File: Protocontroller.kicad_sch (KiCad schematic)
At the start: 37 parts, among them U1 AP2112K-3.3TRG1, U2 PM254-1-14-Z-8.5, U3 PM254-1-14-Z-8.5, U4 SN74AHCT245PWR, U5 SN74AHCT245PWR, U6 SN74AHCT374PWR, U8 2541WR-2X08P, U9 2541WR-2X05P

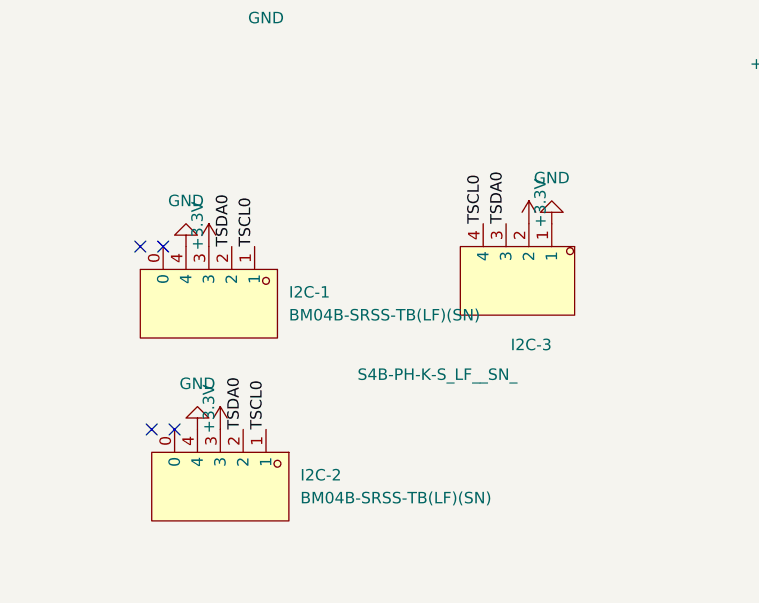
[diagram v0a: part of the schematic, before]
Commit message: Fix I2C, Pathing, and improve Silkscreen
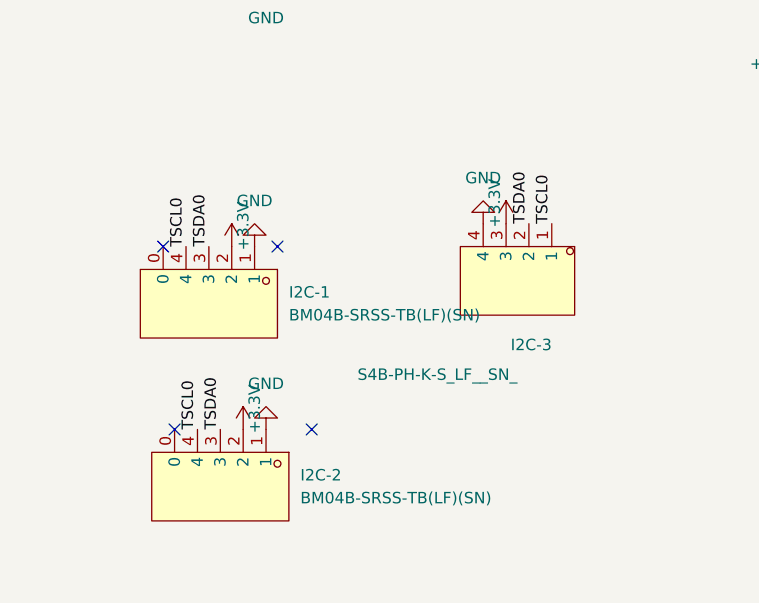
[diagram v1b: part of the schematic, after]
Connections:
- net +3.3V: now also I2C-1.2, I2C-2.2, I2C-3.3; no longer I2C-1.3, I2C-2.3, I2C-3.2
- net GND: now also I2C-1.1, I2C-2.1, I2C-3.4; no longer I2C-1.4, I2C-2.4, I2C-3.1
- net TSCL0: now also I2C-1.4, I2C-2.4, I2C-3.1; no longer I2C-1.1, I2C-2.1, I2C-3.4
- net TSDA0: now also I2C-1.3, I2C-2.3, I2C-3.2; no longer I2C-1.2, I2C-2.2, I2C-3.3
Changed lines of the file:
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@@
 	)
 	(no_connect
-		(at 43.18 135.89)
+		(at 60.96 135.89)
 	)
 	(no_connect
@@
 	)
 	(no_connect
-		(at 44.45 115.57)
+		(at 57.15 115.57)
 	)
 	(no_connect
@@
 	)
 	(no_connect
-		(at 41.91 115.57)
+		(at 44.45 115.57)
 	)
 	(no_connect
@@
 	)
 	(label "TSCL0"
-		(at 54.61 115.57 90)
+		(at 46.99 115.57 90)
 		(effects
 			(font
@@
 	)
 	(label "TSDA0"
-		(at 53.34 135.89 90)
+		(at 50.8 135.89 90)
 		(effects
 			(font
@@
 	)
 	(label "TSCL0"
-		(at 55.88 135.89 90)
+		(at 48.26 135.89 90)
 		(effects
 			(font
@@
 	)
 	(label "TSCL0"
-		(at 80.01 113.03 90)
+		(at 87.63 113.03 90)
 		(effects
 			(font
@@
 	)
 	(label "TSDA0"
-		(at 82.55 113.03 90)
+		(at 85.09 113.03 90)
 		(effects
 			(font
@@
 	)
 	(label "TSDA0"
-		(at 52.07 115.57 90)
+		(at 49.53 115.57 90)
 		(effects
 			(font
@@
 	(symbol
 		(lib_id "power:GND")
-		(at 48.26 135.89 180)
+		(at 55.88 135.89 0)
+		(mirror x)
 		(unit 1)
 		(exclude_from_sim no)
@@
 		(fields_autoplaced yes)
 		(property "Reference" "#PWR020"
-			(at 48.26 129.54 0)
+			(at 55.88 129.54 0)
 			(effects
 				(font
@@
 		)
 		(property "Value" "GND"
-			(at 48.26 130.81 0)
+			(at 55.88 130.81 0)
 			(effects
 				(font
@@
 		)
 		(property "Footprint" ""
-			(at 48.26 135.89 0)
+			(at 55.88 135.89 0)
 			(effects
 				(font
@@
 		)
 		(property "Datasheet" ""
-			(at 48.26 135.89 0)
+			(at 55.88 135.89 0)
 			(effects
 				(font
@@
 		)
 		(property "Description" "Power symbol creates a global label with name \"GND\" , ground"
-			(at 48.26 135.89 0)
+			(at 55.88 135.89 0)
 			(effects
 				(font
@@
 	(symbol
 		(lib_id "power:+3.3V")
-		(at 85.09 113.03 0)
-		(mirror y)
+		(at 82.55 113.03 0)
 		(unit 1)
 		(exclude_from_sim no)
@@
 		(dnp no)
 		(property "Reference" "#PWR0139"
-			(at 85.09 116.84 0)
+			(at 82.55 116.84 0)
 			(effects
 				(font
@@
 		)
 		(property "Value" "+3.3V"
-			(at 86.36 110.744 90)
+			(at 81.28 110.744 90)
 			(effects
 				(font
@@
 		)
 		(property "Footprint" ""
-			(at 85.09 113.03 0)
+			(at 82.55 113.03 0)
 			(effects
 				(font
@@
 		)
 		(property "Datasheet" ""
-			(at 85.09 113.03 0)
+			(at 82.55 113.03 0)
 			(effects
 				(font
@@
 		)
 		(property "Description" "Power symbol creates a global label with name \"+3.3V\""
-			(at 85.09 113.03 0)
+			(at 82.55 113.03 0)
 			(effects
 				(font
@@
 	(symbol
 		(lib_id "power:GND")
-		(at 87.63 113.03 0)
-		(mirror x)
+		(at 80.01 113.03 180)
 		(unit 1)
 		(exclude_from_sim no)
@@
 		(fields_autoplaced yes)
 		(property "Reference" "#PWR0140"
-			(at 87.63 106.68 0)
+			(at 80.01 106.68 0)
 			(effects
 				(font
@@
 		)
 		(property "Value" "GND"
-			(at 87.63 107.95 0)
+			(at 80.01 107.95 0)
 			(effects
 				(font
@@
 		)
 		(property "Footprint" ""
-			(at 87.63 113.03 0)
+			(at 80.01 113.03 0)
 			(effects
 				(font
@@
 		)
 		(property "Datasheet" ""
-			(at 87.63 113.03 0)
+			(at 80.01 113.03 0)
 			(effects
 				(font
@@
 		)
 		(property "Description" "Power symbol creates a global label with name \"GND\" , ground"
-			(at 87.63 113.03 0)
+			(at 80.01 113.03 0)
 			(effects
 				(font
@@
 	(symbol
 		(lib_id "power:GND")
-		(at 46.99 115.57 180)
+		(at 54.61 115.57 0)
+		(mirror x)
 		(unit 1)
 		(exclude_from_sim no)
@@
 		(fields_autoplaced yes)
 		(property "Reference" "#PWR0136"
-			(at 46.99 109.22 0)
+			(at 54.61 109.22 0)
 			(effects
 				(font
@@
 		)
 		(property "Value" "GND"
-			(at 46.99 110.49 0)
+			(at 54.61 110.49 0)
 			(effects
 				(font
@@
 		)
 		(property "Footprint" ""
-			(at 46.99 115.57 0)
+			(at 54.61 115.57 0)
 			(effects
 				(font
@@
 		)
 		(property "Datasheet" ""
-			(at 46.99 115.57 0)
+			(at 54.61 115.57 0)
 			(effects
 				(font
@@
 		)
 		(property "Description" "Power symbol creates a global label with name \"GND\" , ground"
-			(at 46.99 115.57 0)
+			(at 54.61 115.57 0)
 			(effects
 				(font
@@
 	(symbol
 		(lib_id "power:+3.3V")
-		(at 50.8 135.89 0)
+		(at 53.34 135.89 0)
+		(mirror y)
 		(unit 1)
 		(exclude_from_sim no)
@@
 		(dnp no)
 		(property "Reference" "#PWR021"
-			(at 50.8 139.7 0)
+			(at 53.34 139.7 0)
 			(effects
 				(font
@@
 		)
 		(property "Value" "+3.3V"
-			(at 49.53 133.604 90)
+			(at 54.61 133.604 90)
 			(effects
 				(font
@@
 		)
 		(property "Footprint" ""
-			(at 50.8 135.89 0)
+			(at 53.34 135.89 0)
 			(effects
 				(font
@@
 		)
 		(property "Datasheet" ""
-			(at 50.8 135.89 0)
+			(at 53.34 135.89 0)
 			(effects
 				(font
@@
 		)
 		(property "Description" "Power symbol creates a global label with name \"+3.3V\""
-			(at 50.8 135.89 0)
+			(at 53.34 135.89 0)
 			(effects
 				(font
@@
 	(symbol
 		(lib_id "power:+3.3V")
-		(at 49.53 115.57 0)
+		(at 52.07 115.57 0)
+		(mirror y)
 		(unit 1)
 		(exclude_from_sim no)
@@
 		(dnp no)
 		(property "Reference" "#PWR0135"
-			(at 49.53 119.38 0)
+			(at 52.07 119.38 0)
 			(effects
 				(font
@@
 		)
 		(property "Value" "+3.3V"
-			(at 48.26 113.284 90)
+			(at 53.34 113.284 90)
 			(effects
 				(font
@@
 		)
 		(property "Footprint" ""
-			(at 49.53 115.57 0)
+			(at 52.07 115.57 0)
 			(effects
 				(font
@@
 		)
 		(property "Datasheet" ""
-			(at 49.53 115.57 0)
+			(at 52.07 115.57 0)
 			(effects
 				(font
@@
 		)
 		(property "Description" "Power symbol creates a global label with name \"+3.3V\""
-			(at 49.53 115.57 0)
+			(at 52.07 115.57 0)
 			(effects
 				(font

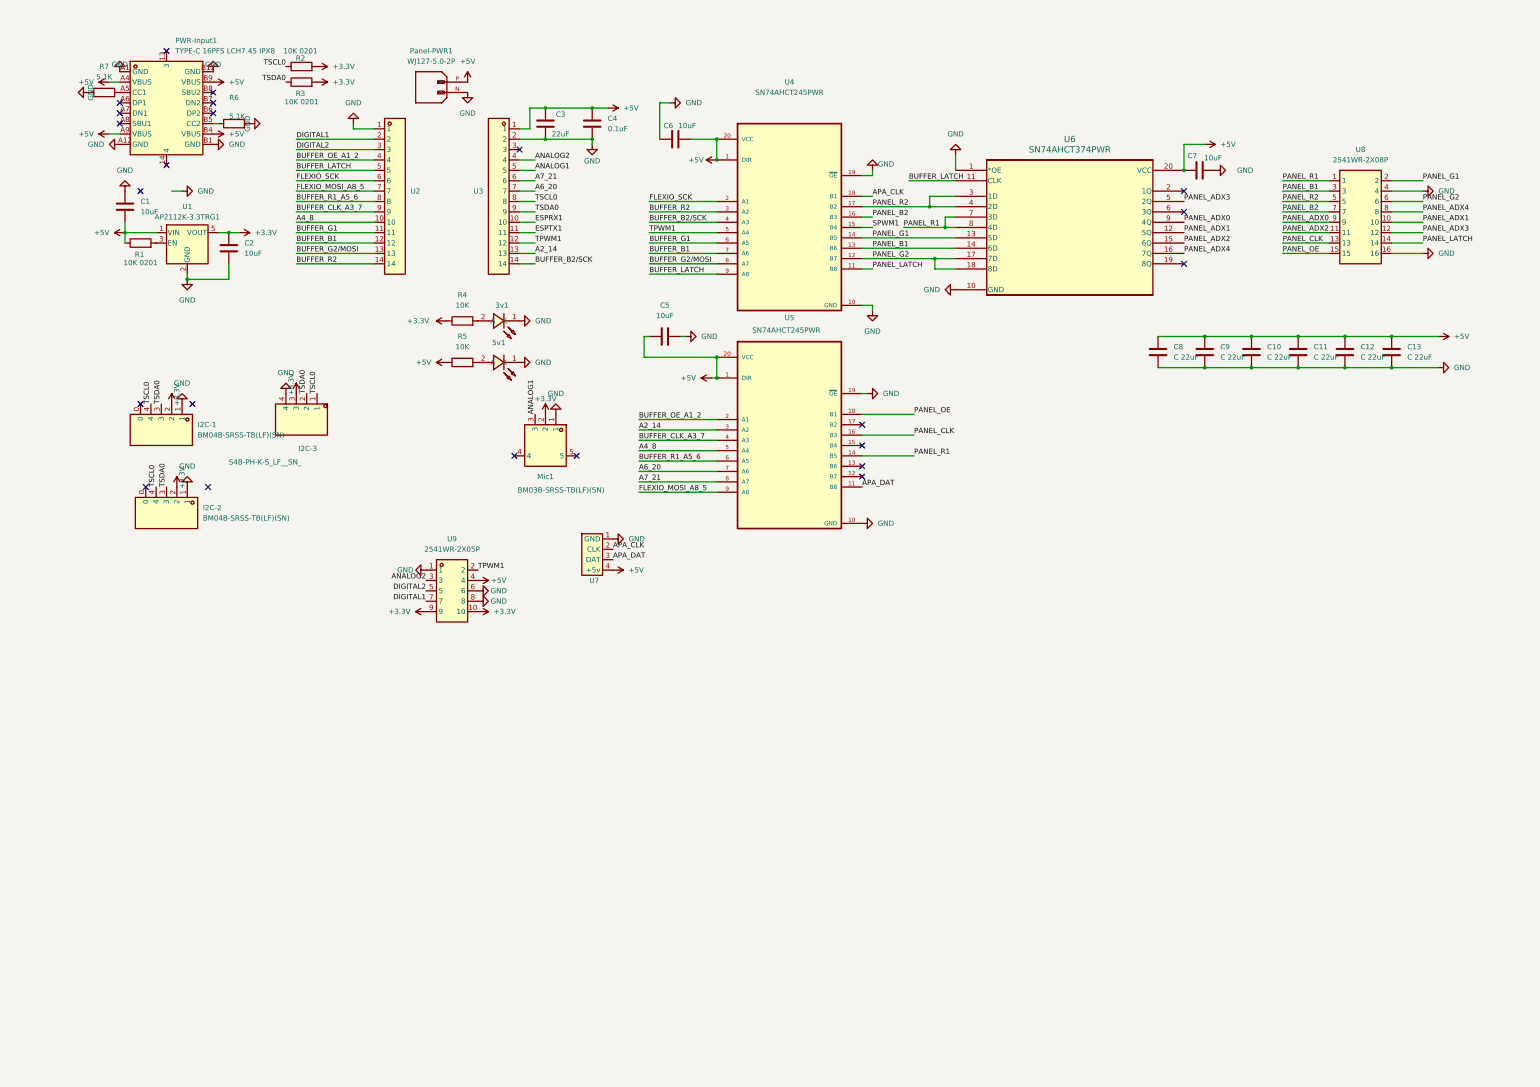
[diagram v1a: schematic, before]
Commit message: Remove WS35 Support, Adjust Traces, Fix issue with Panel out not actually being connected to anything
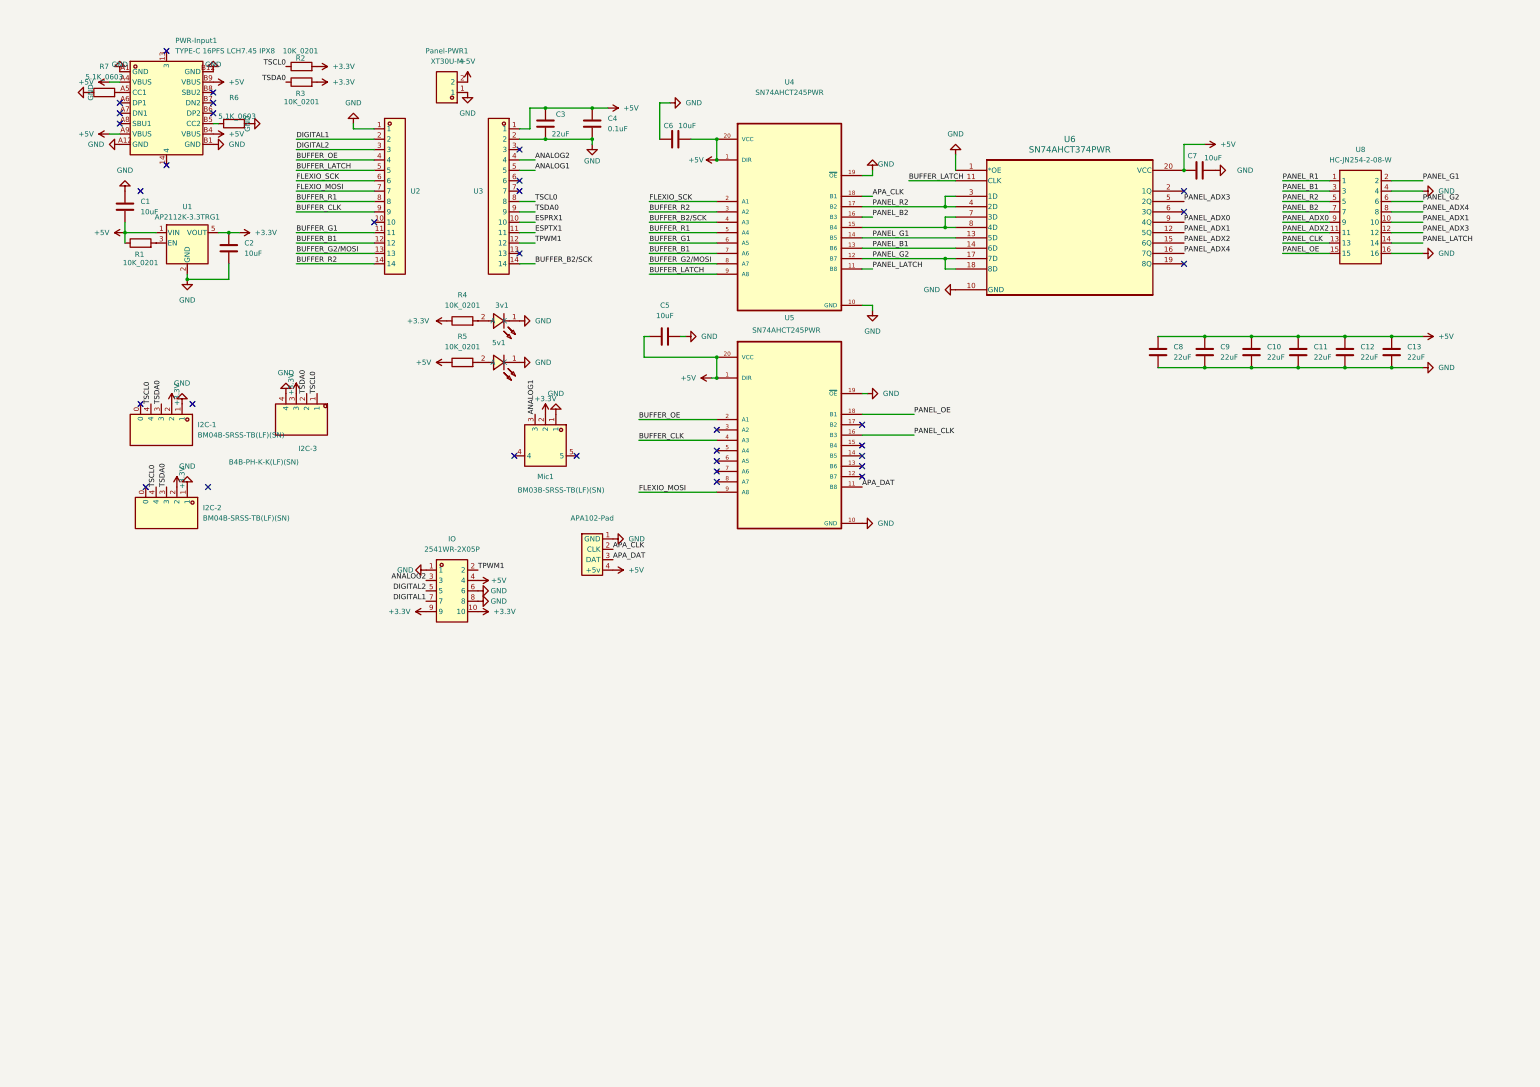
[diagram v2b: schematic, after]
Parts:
- APA102-Pad: renamed from U7; now left out of the parts list
- C1, C2, C5, C6, C7: LCSC Part (none) -> C19702
- C10, C11, C8, C9: value C 22uF -> 22uF; LCSC Part (none) -> C415703
- C12, C13: value C 22uF -> 22uF; LCSC (none) -> C415703
- C3: LCSC Part (none) -> C59461
- C4: LCSC Part (none) -> C1591
- I2C-3: value S4B-PH-K-S_LF__SN_ -> B4B-PH-K-K(LF)(SN)
- Panel-PWR1: value WJ127-5.0-2P -> XT30U-M; symbol XT30PW-M:XT30PW-M -> Protocontroller:XT30U-M; Availability Not in stock -> In Stock; LCSC Part C3703 -> C99101; Rotation Offset (none) -> 180
- R1, R2, R3: value 10K 0201 -> 10K_0201; LCSC Part (none) -> C106225
- R4, R5: value 10K -> 10K_0201; footprint Resistor_SMD:R_01005_0402Metric -> Resistor_SMD:R_0201_0603Metric; LCSC Part (none) -> C106225
- R6, R7: value 5.1K -> 5.1K_0603; footprint Resistor_SMD:R_01005_0402Metric -> Resistor_SMD:R_0603_1608Metric; LCSC Part (none) -> C23186
- U1: LCSC Part (none) -> C51118
- U4, U5: LCSC Part (none) -> C10910
- U6: LCSC Part (none) -> C141313; Rotation Offset (none) -> -90
- U8: value 2541WR-2X08P -> HC-JN254-2-08-W; LCSC Part C3406 -> C5372877
- renumbered U9 to IO
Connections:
- net +5V: now also Panel-PWR1.2; no longer Panel-PWR1.P
- net GND: now also Panel-PWR1.1; no longer Panel-PWR1.N
- net PANEL_R1: no longer U5.14 (B5), U6.7 (3D), U6.8 (4D)
- net TPWM1: no longer U4.5 (A4)
- net A2_14: no longer names the net of U3.13
- net A2_14: no longer U5.3 (A2)
- net A4_8: no longer names the net of U2.10
- net A4_8: no longer U5.5 (A4)
- net A6_20: no longer names the net of U3.7
- net A6_20: no longer U5.7 (A6)
- net A7_21: no longer names the net of U3.6
- net A7_21: no longer U5.8 (A7)
- net BUFFER_CLK_A3_7 renamed BUFFER_CLK
- net BUFFER_OE_A1_2 renamed BUFFER_OE
- net BUFFER_R1_A5_6: no longer names the net of U5.6 (A5)
- net BUFFER_R1_A5_6: no longer U2.8
- net FLEXIO_MOSI_A8_5 renamed FLEXIO_MOSI
- net SPWM1: no longer names the net of U4.15 (B4)
- net SPWM1: now also U6.7 (3D), U6.8 (4D)
- new net BUFFER_R1: U2.8, U4.5 (A4)
- no-connect marks 23 -> 33

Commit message: Fix 3v3 Regulator having bad Rotation, Fix issue of Mic and Led's being replaced when updating from schematic.
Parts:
- 3v1, 5v1: value F.0603.00106/P2-0603W7YS2-06T-001 -> XL-1608UVC-04
- I2C-3: MP S4B-PH-K-S(LF)(SN) -> S4B-PH-K-K(LF)(SN)
- Mic1: footprint Connector_JST:JST_SH_SM03B-SRSS-TB_1x03-1MP_P1.00mm_Horizontal -> Connector_JST:JST_SH_BM03B-SRSS-TB_1x03-1MP_P1.00mm_Vertical; LCSC Part C160403 -> C160389
- renumbered APA102-Pad to APA102-Pad1, IO to IO1
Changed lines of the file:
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@@
 		(dnp no)
 		(fields_autoplaced yes)
-		(property "Reference" "IO"
+		(property "Reference" "IO1"
 			(at 120.65 148.59 0)
 			(effects
@@
 			(project ""
 				(path "/6b9fa612-a115-4864-9524-3b5dfdea87ed"
-					(reference "IO")
+					(reference "IO1")
 					(unit 1)
 				)
@@
 		(dnp no)
 		(fields_autoplaced yes)
-		(property "Reference" "APA102-Pad"
+		(property "Reference" "APA102-Pad1"
 			(at 154.94 143.51 0)
 			(effects
@@
 			(project ""
 				(path "/6b9fa612-a115-4864-9524-3b5dfdea87ed"
-					(reference "APA102-Pad")
+					(reference "APA102-Pad1")
 					(unit 1)
 				)
@@
 			)
 		)
-		(property "MP" "S4B-PH-K-S(LF)(SN)"
+		(property "MP" "S4B-PH-K-K(LF)(SN)"
 			(at 82.55 118.11 0)
 			(effects
@@
 			)
 		)
-		(property "Value" "F.0603.00106/P2-0603W7YS2-06T-001"
+		(property "Value" "XL-1608UVC-04"
 			(at 132.84 101.6 0)
 			(effects
@@
 			)
 		)
-		(property "Value" "F.0603.00106/P2-0603W7YS2-06T-001"
+		(property "Value" "XL-1608UVC-04"
 			(at 132.84 91.44 0)
 			(effects
@@
 			)
 		)
-		(property "Footprint" "Connector_JST:JST_SH_SM03B-SRSS-TB_1x03-1MP_P1.00mm_Horizontal"
+		(property "Footprint" "Connector_JST:JST_SH_BM03B-SRSS-TB_1x03-1MP_P1.00mm_Vertical"
 			(at 128.27 123.19 0)
 			(effects
@@
 			)
 		)
-		(property "LCSC Part" "C160403"
+		(property "LCSC Part" "C160389"
 			(at 123.19 123.19 0)
 			(effects

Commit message: Switch Pullups to use 4.7k Resistors for improved speeds, Adjusted capacitors, removed Designators file
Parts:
- C4: LCSC Part C1591 -> C14663
- R2: value 10K_0201 -> 4.7K_402; footprint Resistor_SMD:R_0201_0603Metric -> Resistor_SMD:R_0402_1005Metric; LCSC Part C106225 -> C25900
- R3: value 10K_0201 -> 4.7K_0402; footprint Resistor_SMD:R_0201_0603Metric -> Resistor_SMD:R_0402_1005Metric; LCSC Part C106225 -> C25900
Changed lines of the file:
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@@
 			)
 		)
-		(property "Value" "10K_0201"
+		(property "Value" "4.7K_0402"
 			(at 83.82 41.656 90)
 			(effects
@@
 			)
 		)
-		(property "Footprint" "Resistor_SMD:R_0201_0603Metric"
+		(property "Footprint" "Resistor_SMD:R_0402_1005Metric"
 			(at 83.82 38.608 90)
 			(effects
@@
 			)
 		)
-		(property "LCSC Part" "C106225"
+		(property "LCSC Part" "C25900"
 			(at 83.82 36.83 0)
 			(effects
@@
 			)
 		)
-		(property "LCSC Part" "C1591"
+		(property "LCSC Part" "C14663"
 			(at 154.94 46.99 0)
 			(effects
@@
 			)
 		)
-		(property "Value" "10K_0201"
+		(property "Value" "4.7K_402"
 			(at 83.566 29.21 90)
 			(effects
@@
 			)
 		)
-		(property "Footprint" "Resistor_SMD:R_0201_0603Metric"
+		(property "Footprint" "Resistor_SMD:R_0402_1005Metric"
 			(at 83.82 34.798 90)
 			(effects
@@
 			)
 		)
-		(property "LCSC Part" "C106225"
+		(property "LCSC Part" "C25900"
 			(at 83.82 33.02 0)
 			(effects

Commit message: Fix Economic Again, fix R1 not being connected, V2 tba
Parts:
- IO1: footprint Protocontroller:HDR-TH_10P-P2.54-H-M-R2-C5-S2.54-N -> Protocontroller:HDR-TH_10P-P2.54-H-F-R2-C5-W12.7-N; symbol Protocontroller:2541WR-2X05P -> Protocontroller:FH-00843; LCSC Part C5383090 -> C2685127
- PWR-Input1: value TYPE-C 16PFS LCH7.45 IPX8 -> TYPE-C 6PLCH10.0 073; footprint Protocontroller:USB-TH_TYPE-C-16PFS-LCH7.45-IPX8 -> Protocontroller:USB-C-TH_TYPE-C-6PLCH10.0-073; symbol Protocontroller:TYPE-C16PFSLCH7.45IPX8 -> Protocontroller:TYPE-C6PLCH10.0073; LCSC Part C3020054 -> C5156601
- U4, U5: value SN74AHCT245PWR -> 74245PW
- U6: value SN74AHCT374PWR -> 74374PW
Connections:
- net +5V: no longer PWR-Input1.A4 (VBUS), PWR-Input1.B4 (VBUS)
- net DIGITAL1: now also IO1.5; no longer IO1.7
- net DIGITAL2: now also IO1.8; no longer IO1.5
- net GND: now also IO1.7; no longer IO1.8, PWR-Input1.A1 (GND), PWR-Input1.B1 (GND)
- net PANEL_R1: now also U4.15 (B4), U6.7 (3D), U6.8 (4D)
- no-connect marks 33 -> 24
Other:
- note added: "(Its 2 Seperate Connectors to look like a Single item)"
- note added: "I2c Connectors and Pullups"
- note added: "Led Connectors"
- note added: "Matrix Data and APA102 Buffers"
- note added: "Mic And IO"
- note added: "Power"
- note added: "Teensy 4.0"
- title: (none) -> Protocontroller Neo
- moved on the sheet: 3v1, 5v1, APA102-Pad1, C1, C10, C11, C12, C13, C2, C3, C4, C5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
